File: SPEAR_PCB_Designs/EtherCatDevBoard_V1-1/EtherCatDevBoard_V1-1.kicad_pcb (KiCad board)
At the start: 4 copper layers, 44 x 55 mm, 116 parts, among them J1 USB_C_Receptacle_USB2.0_16P, J2 FTSH-107-01-F-DV-K-P-TR, J3 Conn_01x20_Pin, J4 Conn_01x20_Pin, J5 SM04B-GHS-TB, J6 SM04B-GHS-TB, SW1 SW_Push, T1 H1102NLT, T2 H1102NLT, U1 USBLC6-2SC6, U2 STM32F446RCT6, U3 AMS1117-3.3 SOT-223, U4 LAN9252I/ML, U5 24FC512-I/SN, U6 TPS2116DRL, Y1 16MHz, Y2 25MHz

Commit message: Updates to V1.1 for Ecat dev board.
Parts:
- Y1: footprint Crystal:Crystal_SMD_3225-4Pin_3.2x2.5mm -> Crystal:Crystal_SMD_2520-4Pin_2.5x2.0mm
- moved C37 67.7 mm to (144.8, 126.7)
- moved R17 66.7 mm to (144.8, 124.2)
- moved R20 66.3 mm to (143.3, 124.2)
- moved R18 65.0 mm to (139.4, 101.6)
- moved J6 54.7 mm to (156.0, 125.7)
- moved T2 54.6 mm to (156.0, 117.1)
- moved R30 54.6 mm to (148.8, 124.2)
- moved G*** 54.5 mm to (156.0, 117.1)
- moved C38 54.3 mm to (132.3, 105.7)
- moved R31 54.3 mm to (147.3, 124.2)
- moved C40 54.3 mm to (147.3, 126.7)
- moved R15 54.1 mm to (132.3, 104.4)
- moved C1 53.9 mm to (154.8, 97.6)
- moved C11 53.9 mm to (139.8, 95.5)
- moved C16 53.9 mm to (134.1, 104.1)
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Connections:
- U2 pad 24: /LAN9252/CS -> /LAN9252/SCS
- U4 pad 28: /LAN9252/CS -> unconnected-(U4-CS-Pad28)
- U4 pad 50: unconnected-(U4-D5-Pad50) -> /LAN9252/SCS
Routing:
- net GND: track 87.5 -> 3.48 mm, vias 72 -> 6
- net +3.3V: track 52.9 -> 0.00 mm, vias 27 -> 0
- net /STM32F446RC/PC0: track 50.1 -> 0.00 mm, vias 1 -> 0
- net /STM32F446RC/PC1: track 49.8 -> 0.00 mm, vias 1 -> 0
- net /STM32F446RC/PC2: track 49.7 -> 0.00 mm, vias 1 -> 0
- net /STM32F446RC/PC3: track 48.7 -> 0.00 mm, vias 1 -> 0
- net /STM32F446RC/PA0: track 45.8 -> 0.00 mm, vias 1 -> 0
- net /STM32F446RC/PC14: track 44.8 -> 0.00 mm, vias 1 -> 0
- net /LAN9252/GPIO1: track 43.6 -> 0.00 mm, vias 2 -> 0
- net /STM32F446RC/PA1: track 43.5 -> 0.00 mm, vias 1 -> 0
- net /STM32F446RC/PC13: track 42.4 -> 0.00 mm, vias 1 -> 0
- net /STM32F446RC/PB8: track 39.5 -> 0.00 mm, vias 1 -> 0
- net /STM32F446RC/PB9: track 38.8 -> 0.00 mm, vias 1 -> 0
- net /STM32F446RC/PA4: track 37.9 -> 0.00 mm, vias 1 -> 0
- net /STM32F446RC/PB7: track 37.1 -> 0.00 mm, vias 1 -> 0
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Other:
- outline, holes or cut-outs redrawn
- board text added: "Version 1.1"
- board text removed: "Version 1.0"

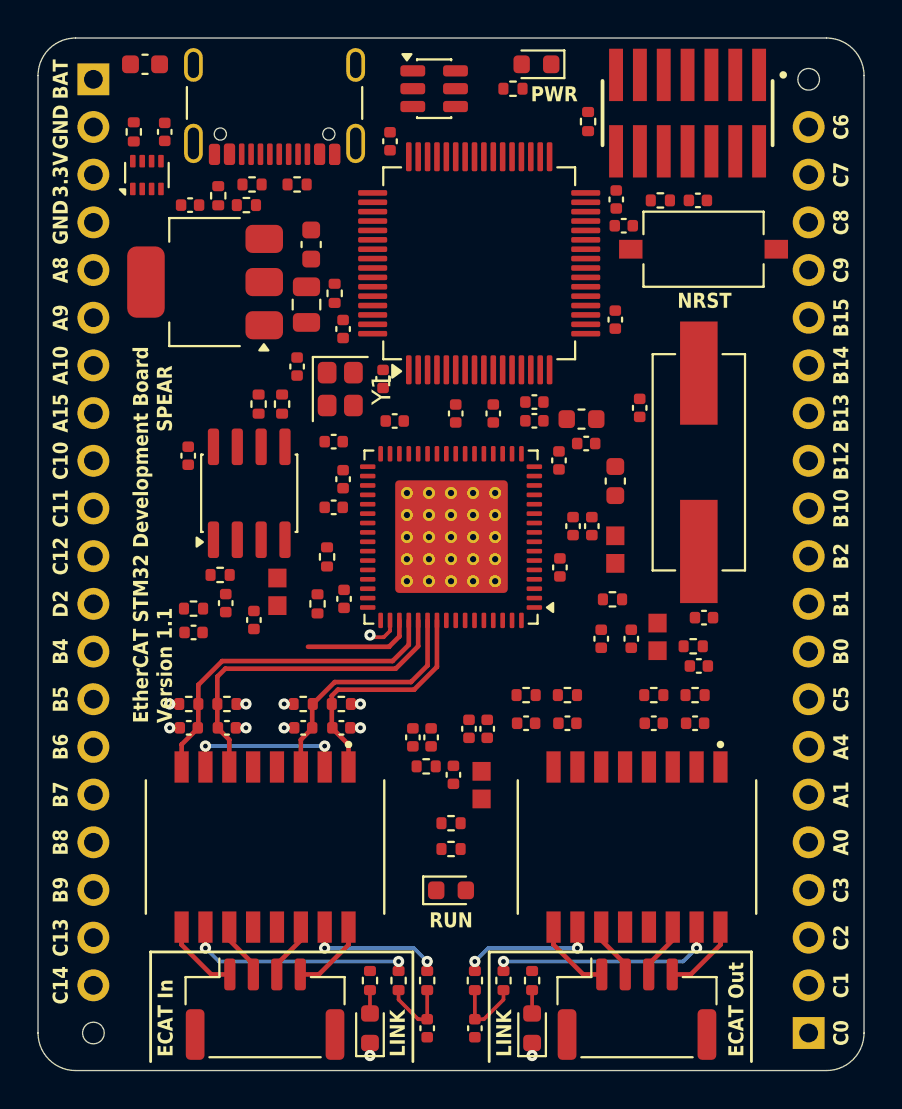
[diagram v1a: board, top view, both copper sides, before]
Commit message: Finished the Ecat Dev Boar V1.1. Fabrication files are available.
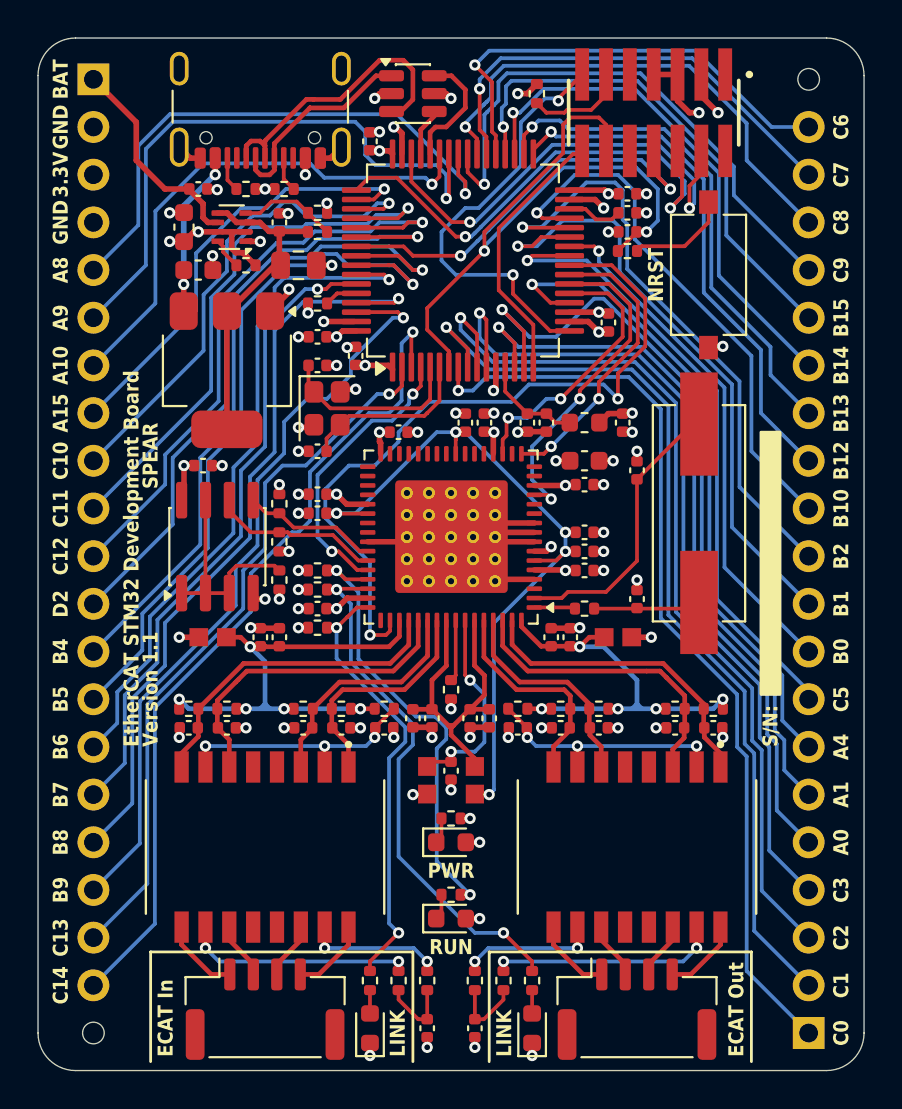
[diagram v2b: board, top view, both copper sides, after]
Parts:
- moved D1 41.7 mm to (146.1, 116.8), turned to 0 degrees
- moved R6 39.0 mm to (146.1, 115.6), turned to 0 degrees
- moved R16 15.2 mm to (138.9, 102.4), turned to 180 degrees
- moved FB2 14.4 mm to (147.3, 113.5), turned to -90 degrees
- moved R15 11.5 mm to (142.5, 109.7), turned to 0 degrees
- moved C38 11.4 mm to (142.5, 110.7), turned to 0 degrees
- moved C41 10.2 mm to (149.6, 110.7), turned to 180 degrees
- moved R29 9.92 mm to (149.6, 109.7), turned to 180 degrees
- moved R34 9.29 mm to (135.1, 86.1), turned to 0 degrees
- moved C52 8.92 mm to (131.8, 84.1), turned to 90 degrees
- moved R21 7.42 mm to (136.9, 100.8), turned to 90 degrees
- moved C14 6.16 mm to (132.6, 86.4), turned to 0 degrees
- moved R32 5.63 mm to (138.9, 84.3), turned to 180 degrees
- moved R22 5.31 mm to (136.9, 98.8)
- moved U6 5.30 mm to (134.4, 84.1), turned to 180 degrees
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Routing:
- net GND: track 3.48 -> 60.2 mm, vias 6 -> 70
- net /STM32F446RC/PC1: track 0.00 -> 50.1 mm, vias 0 -> 1
- net /STM32F446RC/PC0: track 0.00 -> 49.5 mm, vias 0 -> 1
- net /STM32F446RC/PC2: track 0.00 -> 48.1 mm, vias 0 -> 1
- net /STM32F446RC/PC3: track 0.00 -> 45.5 mm, vias 0 -> 1
- net /STM32F446RC/PC14: track 0.00 -> 44.6 mm, vias 0 -> 1
- net /STM32F446RC/PA1: track 0.00 -> 41.3 mm, vias 0 -> 1
- net /STM32F446RC/PB8: track 0.00 -> 40.9 mm, vias 0 -> 1
- net /STM32F446RC/PB9: track 0.00 -> 40.9 mm, vias 0 -> 1
- net /STM32F446RC/PA0: track 0.00 -> 40.6 mm, vias 0 -> 1
- net /STM32F446RC/PB5: track 0.00 -> 38.5 mm, vias 0 -> 1
- net /STM32F446RC/PC13: track 0.00 -> 38.4 mm, vias 0 -> 1
- net /LAN9252/SCS: track 1.82 -> 39.7 mm, vias 1 -> 2
- net /LAN9252/VDDCR: track 0.00 -> 37.3 mm, vias 0 -> 5
- net /STM32F446RC/PB4: track 0.00 -> 37.2 mm, vias 0 -> 1
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- removed copper zone on In2.Cu, net +5V
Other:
- board text added: "S/N:"

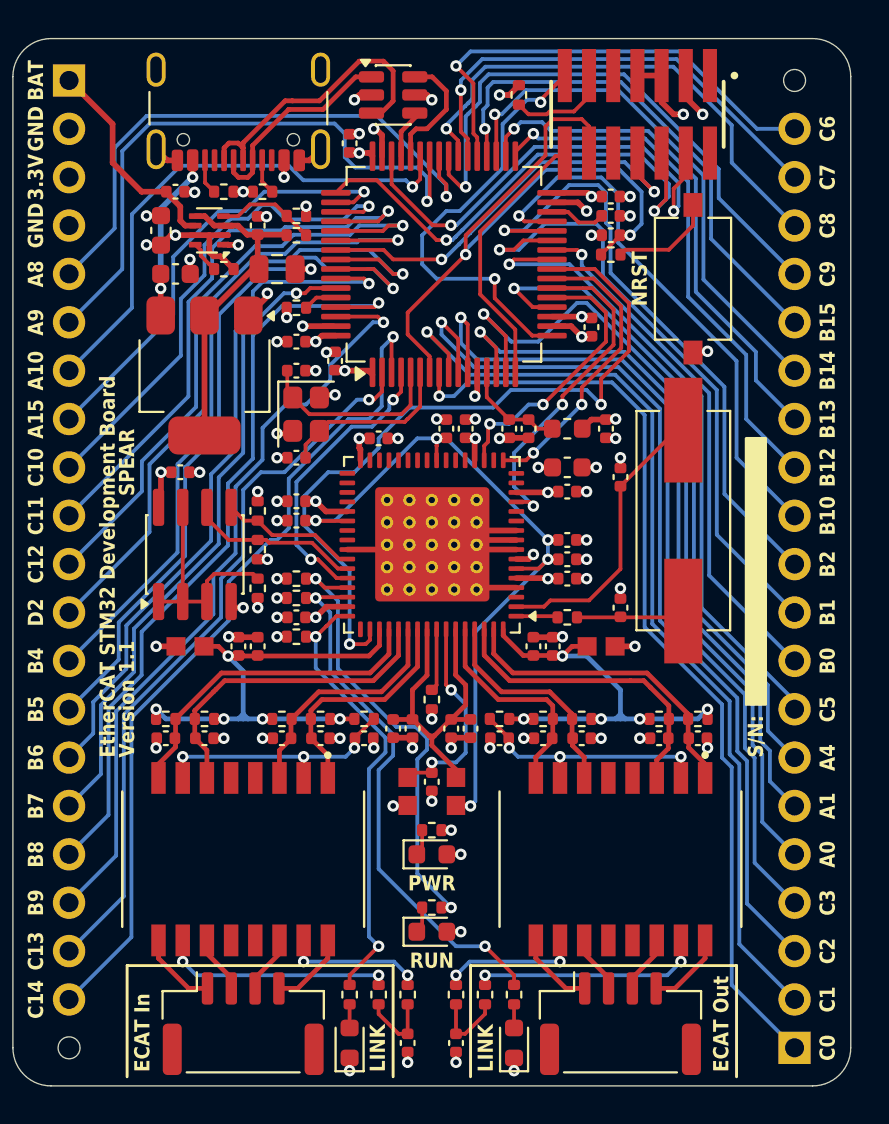
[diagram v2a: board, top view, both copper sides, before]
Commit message: Updated Ecat dev board v1.1 to use vias with hole size 0.3mm and diameter 0.45mm to match jlcpcb. Also moved vias to avoid solder mask openings to prevent solder wicking.
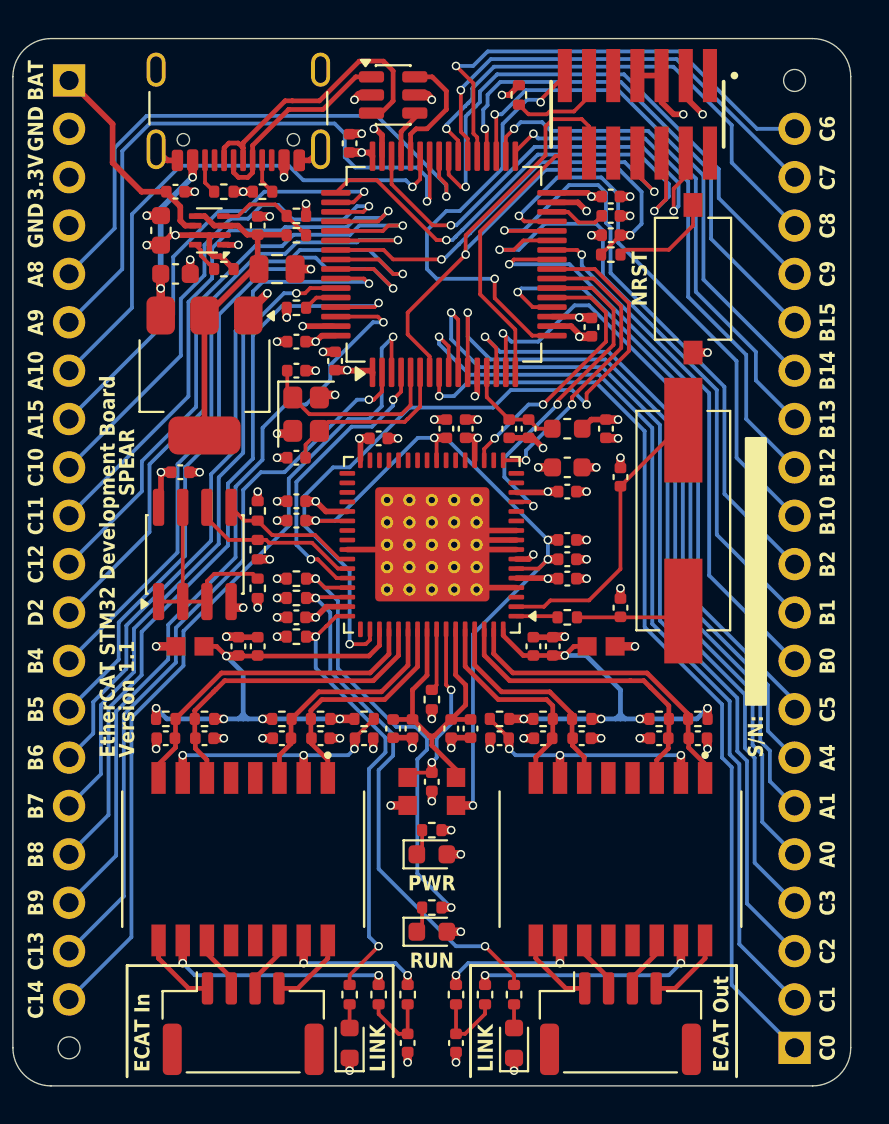
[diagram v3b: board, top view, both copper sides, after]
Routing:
- net GND: track 60.2 -> 86.4 mm
- net +3.3V: track 35.3 -> 44.3 mm
- net /STM32F446RC/PA1: track 41.3 -> 38.4 mm
- net /LAN9252/VDD33TXRX1: track 25.0 -> 27.7 mm
- net /LAN9252/VDD33TXRX2: track 21.5 -> 24.0 mm
- net /LAN9252/VDDCR: track 37.3 -> 39.7 mm
- net /STM32F446RC/PC1: track 50.1 -> 48.6 mm
- net Net-(U4-VDD33BIAS): track 10.8 -> 9.43 mm
- net /STM32F446RC/PA0: track 40.6 -> 39.4 mm
- net /LAN9252/GPIO2: track 23.1 -> 24.1 mm
- net /LAN9252/SCS: track 39.7 -> 38.9 mm
- net /STM32F446RC/PC3: track 45.5 -> 44.8 mm
- net Net-(C38-Pad1): track 12.9 -> 13.5 mm
- net Net-(C41-Pad1): track 12.9 -> 13.5 mm
- net /LAN9252/SCK: track 14.6 -> 14.0 mm
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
